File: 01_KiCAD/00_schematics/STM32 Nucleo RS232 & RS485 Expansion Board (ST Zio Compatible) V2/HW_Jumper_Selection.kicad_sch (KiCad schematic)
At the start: 77 parts, among them J10 DIR, J11 TERM_TX, J12 TERM_RX, J13 SLR, J7 MODE0, J8 MODE1, J9 MODE2, U10 SN74LVC2G14DBV, U11 SN74LVC2G14DBV, U5 SN74LVC2G14DBV, U6 SN74LVC2G14DBV, U7 SN74LVC2G14DBV, U8 SN74LVC2G14DBV, U9 SN74LVC2G14DBV

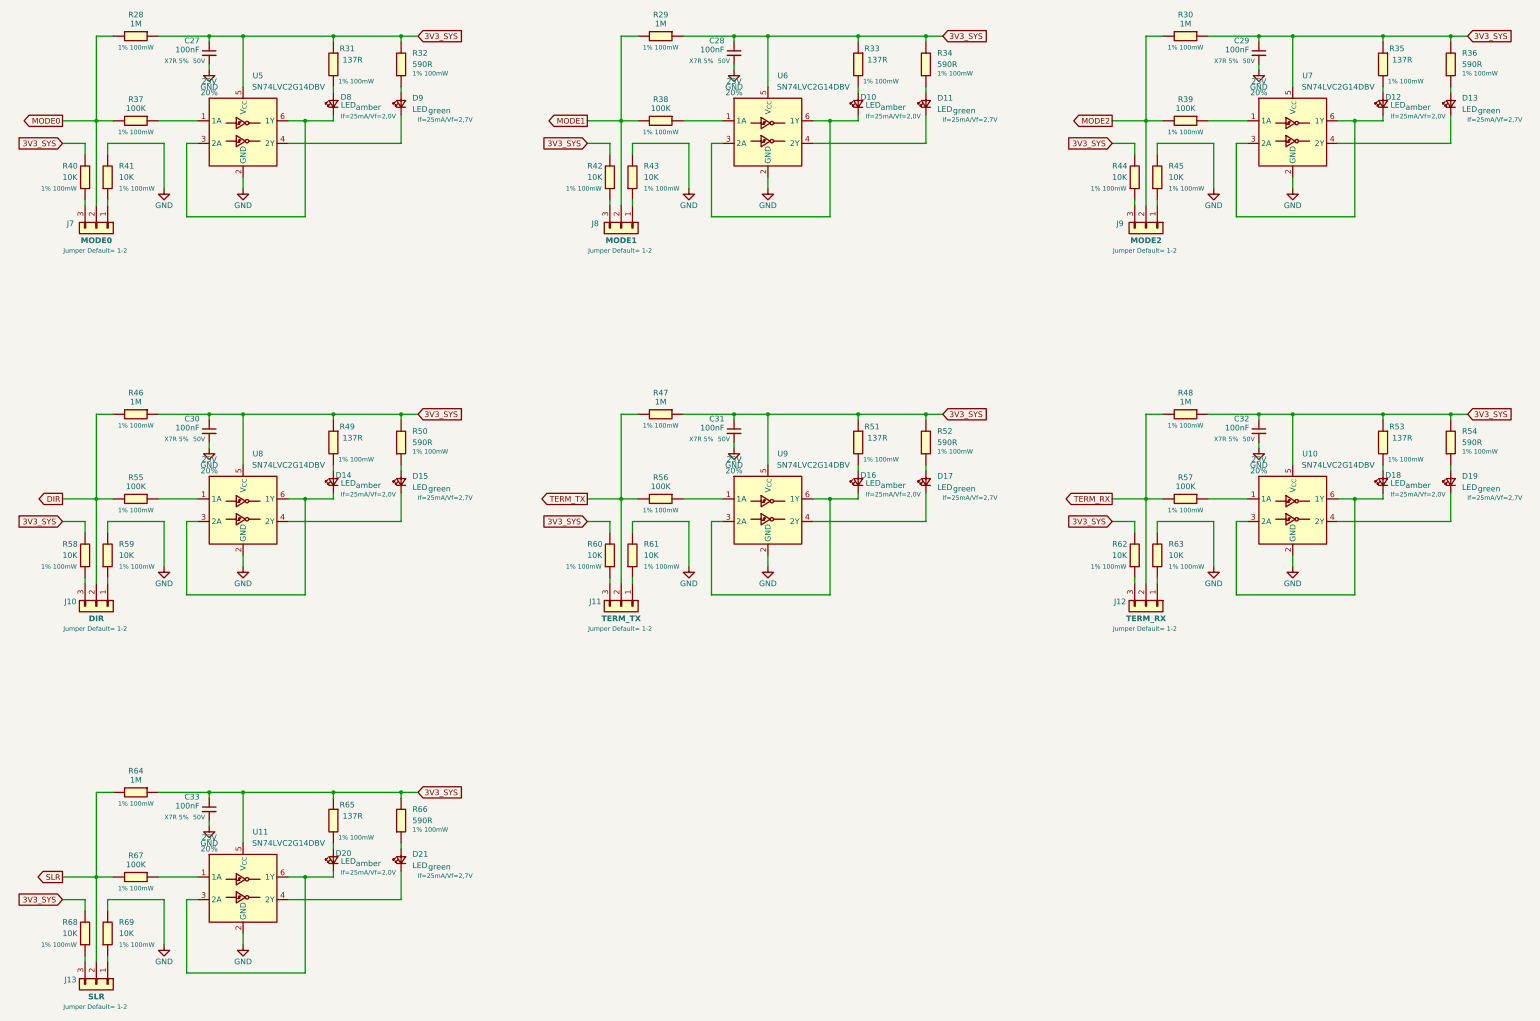
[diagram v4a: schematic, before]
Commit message: Changed schmitt trigger
changed the schmitt trigger for hex-schmitt trigger variant to simpify design and reduce components
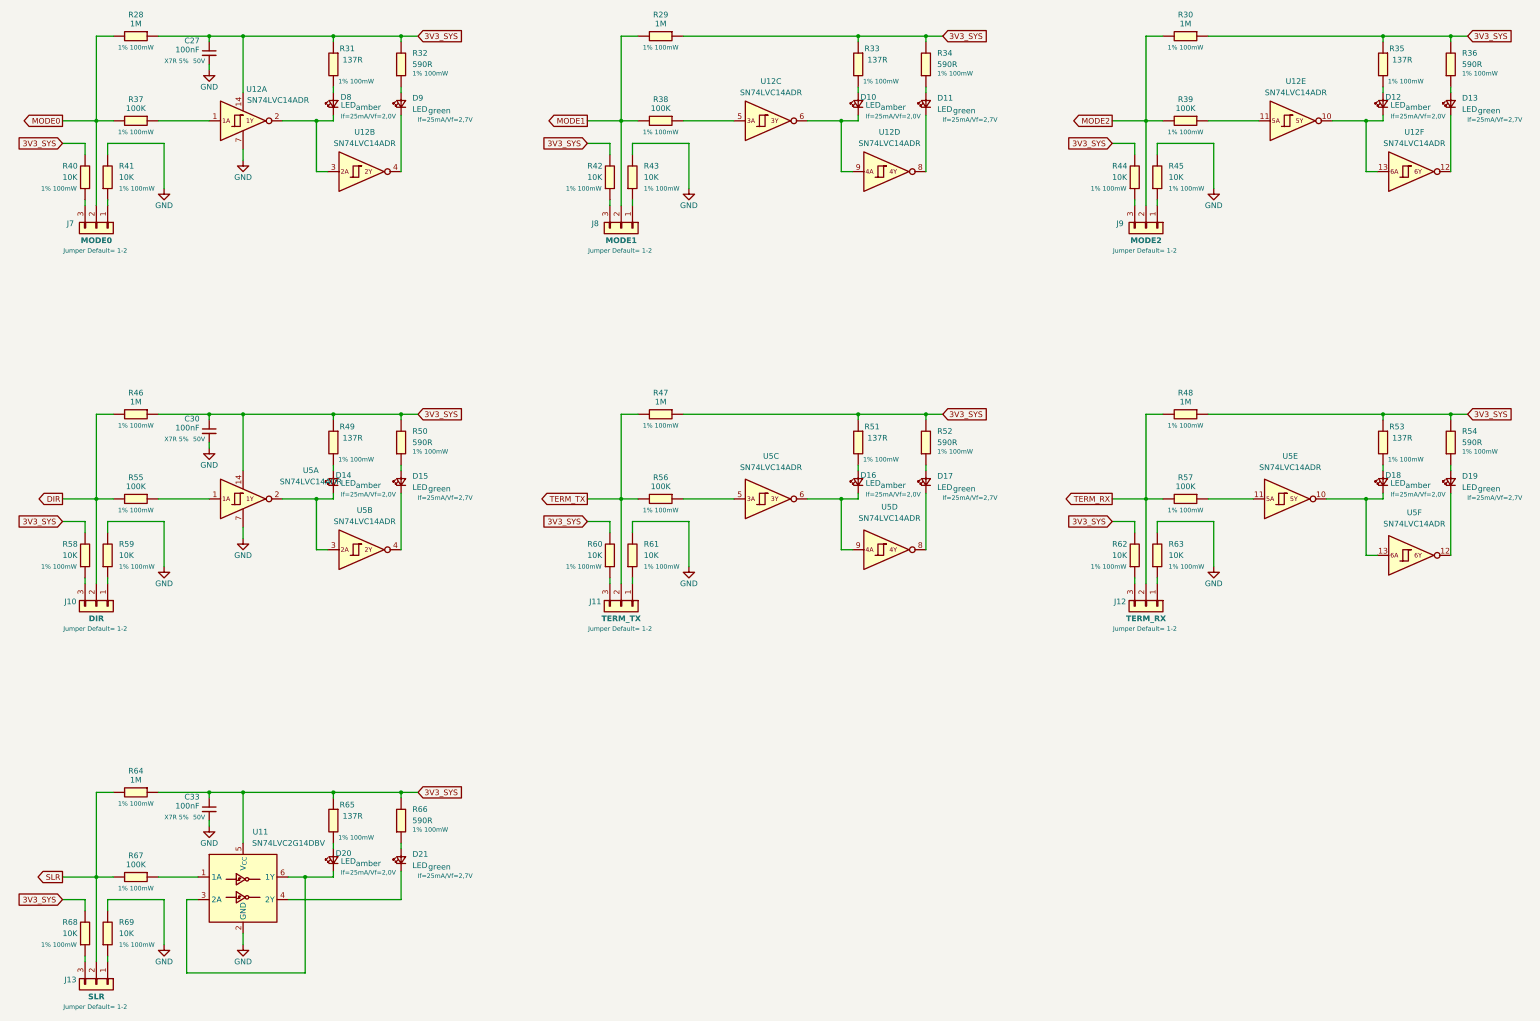
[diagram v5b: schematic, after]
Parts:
- removed C28, C29, C31, C32: 100nF, PCM_SparkFun-Capacitor:C_0603_1608Metric, symbol PCM_SparkFun-Capacitor:0.1uF_0603_25V_20%
- removed U10, U5, U6, U7, U8, U9: SN74LVC2G14DBV, Package_TO_SOT_SMD:SOT-23-6, symbol 74xGxx:SN74LVC2G14DBV
- added U12, U5: SN74LVC14ADR, SN74LVC14ADR:SOIC127P600X175-14N, symbol SN74LVC14A:SN74LVC14ADR
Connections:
- net 3V3_SYS: now also U12.14 (VCC), U5.14 (VCC)
- net GND: now also U12.7 (GND), U5.7 (GND)
- net at R55.2: now also U5.1 (1A)
- net at D14.1 (K): now also U5.2 (1Y), U5.3 (2A)
- net at D15.1 (K): now also U5.4 (2Y)
- net at R39.2: now also U12.11 (5A)
- net at D12.1 (K): now also U12.10 (5Y), U12.13 (6A)
- net at D13.1 (K): now also U12.12 (6Y)
- net at R38.2: now also U12.5 (3A)
- net at D17.1 (K): now also U5.8 (4Y)
- net at R57.2: now also U5.11 (5A)
- net at D16.1 (K): now also U5.6 (3Y), U5.9 (4A)
- net at R56.2: now also U5.5 (3A)
- net at R37.2: now also U12.1 (1A)
- net at D8.1 (K): now also U12.2 (1Y), U12.3 (2A)
- net at D9.1 (K): now also U12.4 (2Y)
- net at D19.1 (K): now also U5.12 (6Y)
- net at D10.1 (K): now also U12.6 (3Y), U12.9 (4A)
- net at D11.1 (K): now also U12.8 (4Y)
- net at D18.1 (K): now also U5.10 (5Y), U5.13 (6A)

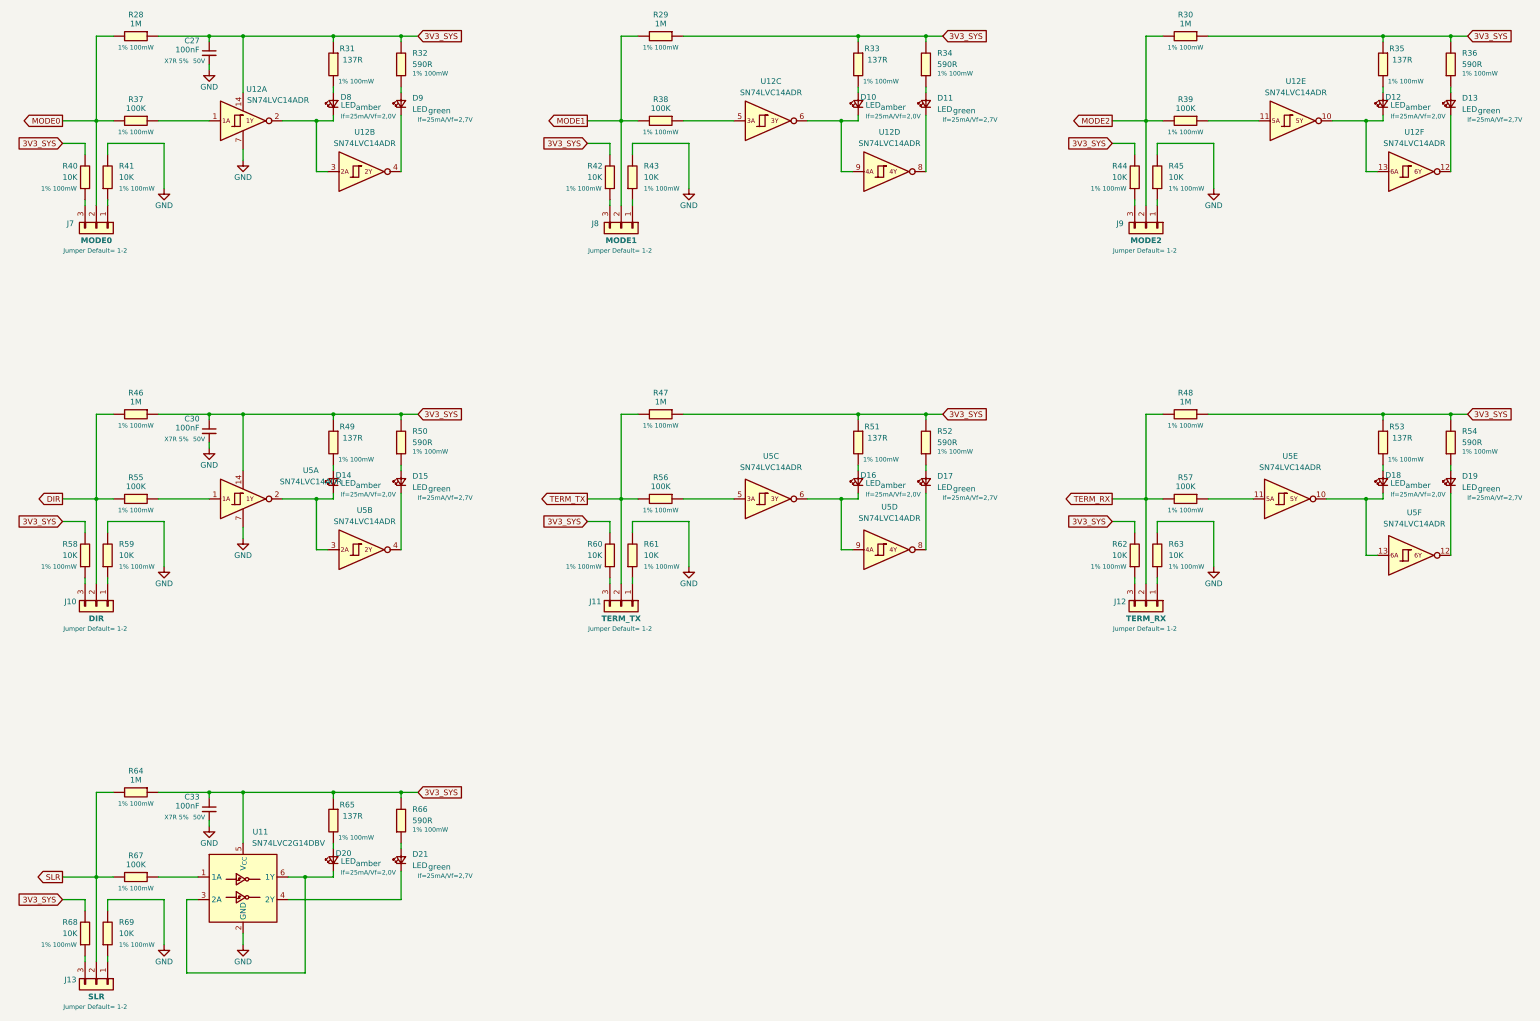
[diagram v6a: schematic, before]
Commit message: Complete redesign
Redesigned the complete board. Added hardware termination jumpers for 1120R resistors for RS485. Changes footprint, package size and simplified values between capacitors.
Still need to re-route the entire board :-(
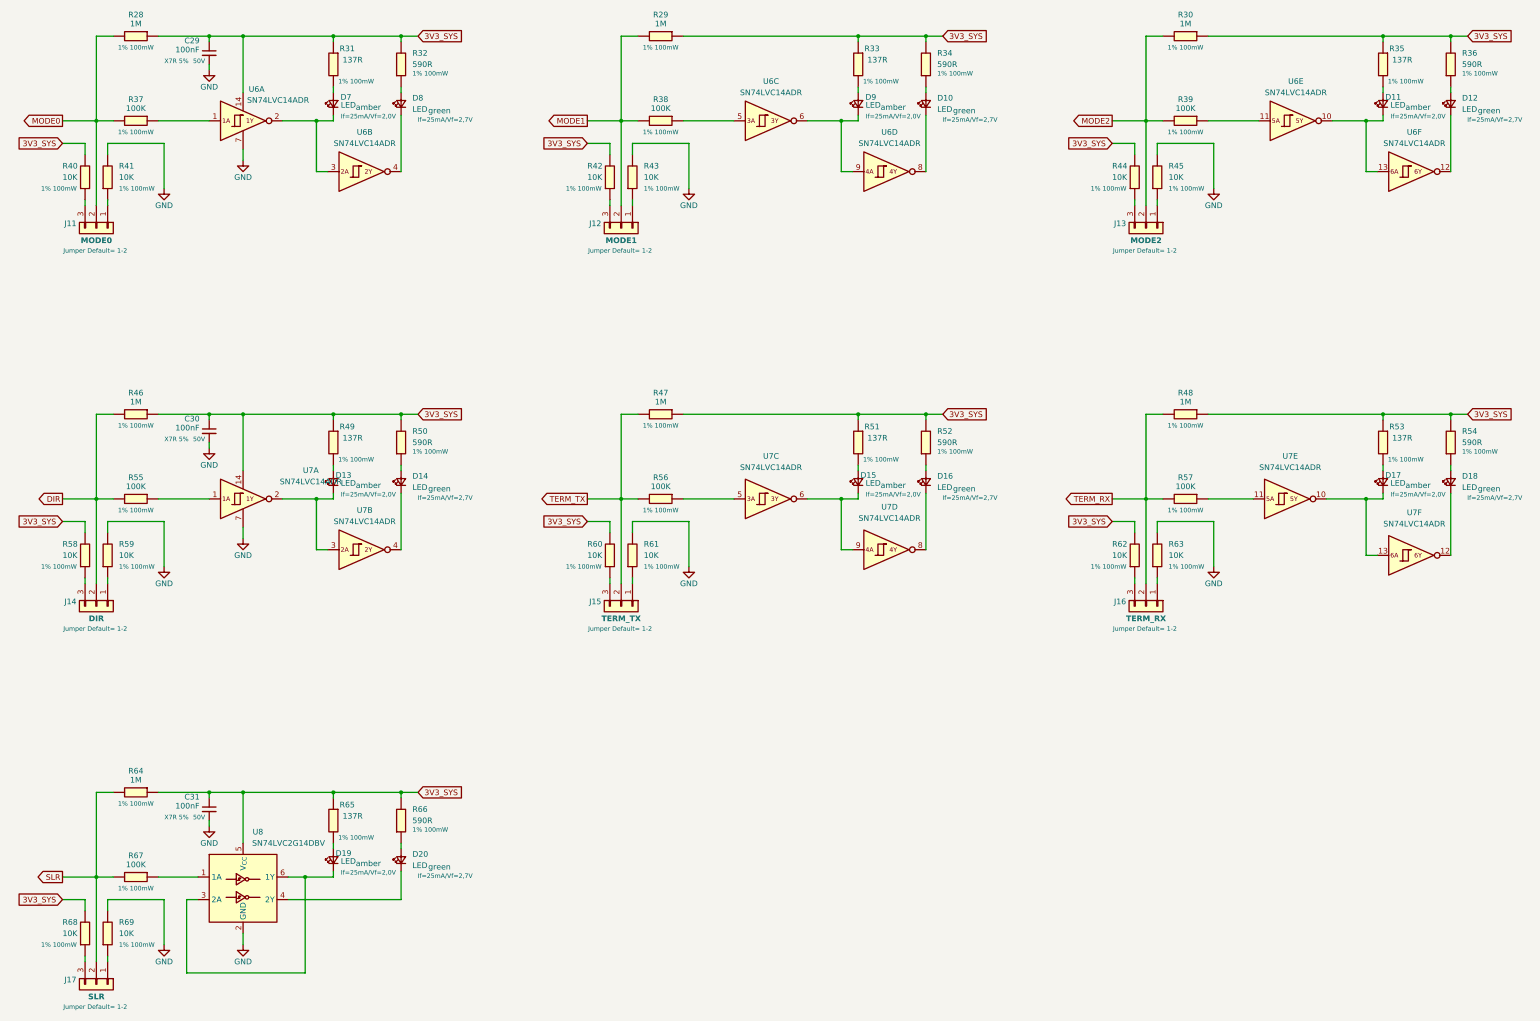
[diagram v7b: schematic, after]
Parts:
- renumbered C27 to C29, C33 to C31, D11 to D10, D12 to D11, D13 to D12, D14 to D13, D15 to D14, D16 to D15, D17 to D16, D18 to D17, D19 to D18, D20 to D19, D21 to D20, D8 to D7, D9 to D8, D10 to D9, J7 to J11, J8 to J12, J9 to J13, J10 to J14, J11 to J15, J12 to J16, J13 to J17, U12 to U6, U5 to U7, U11 to U8
